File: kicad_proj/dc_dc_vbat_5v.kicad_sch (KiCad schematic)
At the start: 19 parts, among them Q1 DMG2305UX-7, U4 TPS563200, U7 DMMT5401-7-F

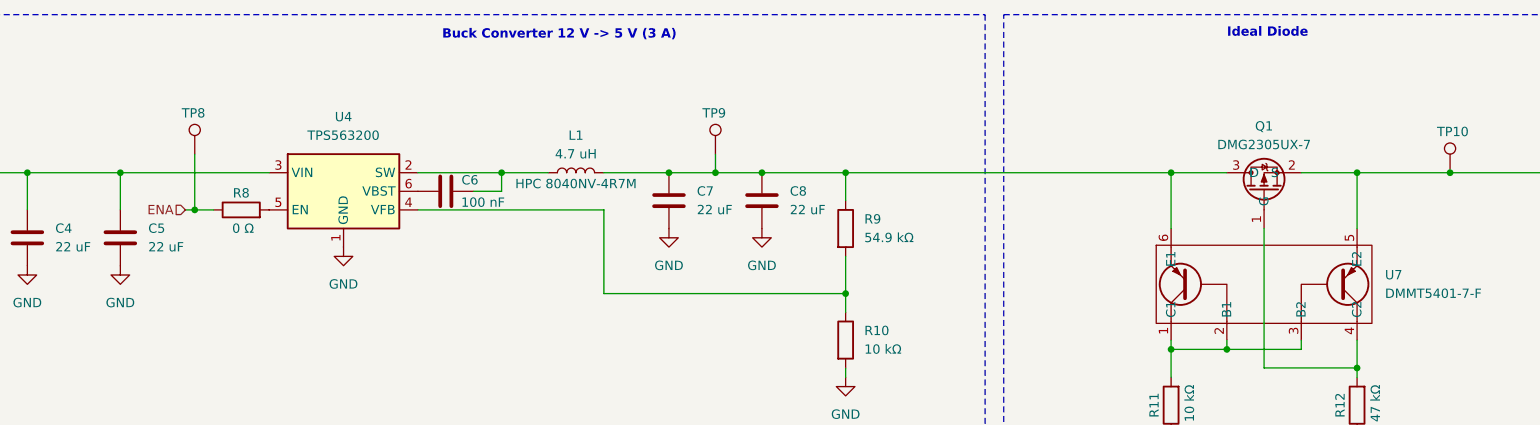
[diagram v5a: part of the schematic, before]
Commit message: progress a bit with the placement an replace 5 v buck converter L for a smaller one
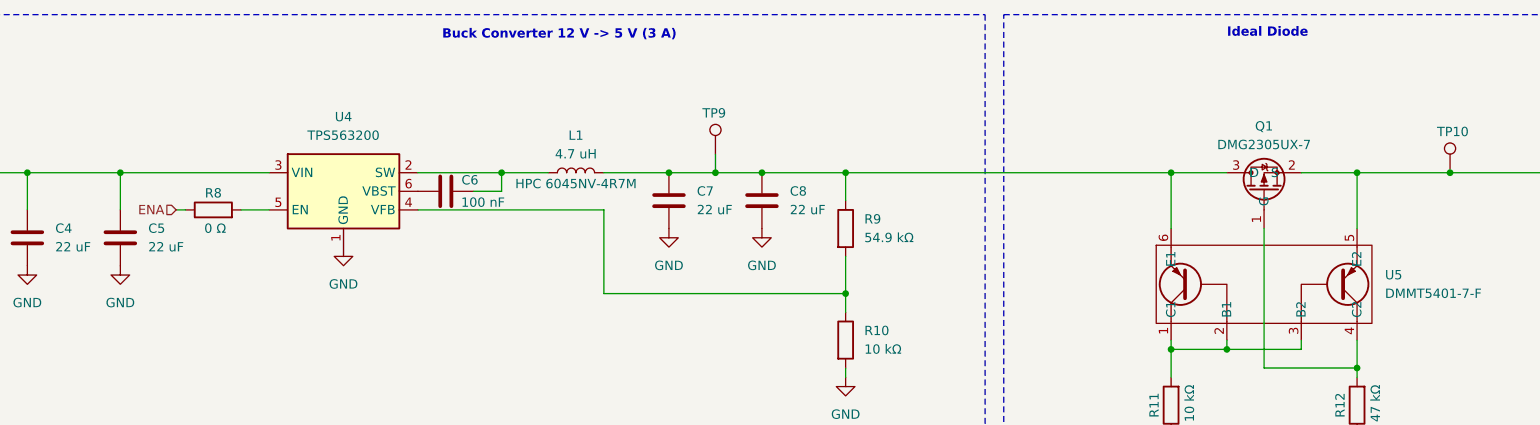
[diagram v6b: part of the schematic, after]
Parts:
- removed TP8: TestPoint, TestPoint:TestPoint_Pad_D2.5mm, symbol Connector:TestPoint
- L1: footprint rpi_power_warden_hat:L_8040_8x8x4mm -> rpi_power_warden_hat:L_6045_6x6x4mm; mpn HPC 8040NV-4R7M -> HPC 6045NV-4R7M
- renumbered U7 to U5
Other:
- moved on the sheet: R8
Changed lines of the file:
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@@
 	)
 	(junction
-		(at 69.85 90.17)
-		(diameter 0)
-		(color 0 0 0 0)
-	)
-	(junction
 		(at 228.6 111.76)
 		(diameter 0)
@@
 	(wire
 		(pts
-			(xy 68.58 90.17) (xy 69.85 90.17)
+			(xy 210.82 109.22) (xy 220.98 109.22)
 		)
 		(stroke
@@
 	(wire
 		(pts
-			(xy 210.82 109.22) (xy 220.98 109.22)
+			(xy 228.6 107.95) (xy 228.6 111.76)
 		)
 		(stroke
@@
 	(wire
 		(pts
-			(xy 228.6 107.95) (xy 228.6 111.76)
+			(xy 147.32 85.09) (xy 158.75 85.09)
 		)
 		(stroke
@@
 	(wire
 		(pts
-			(xy 147.32 85.09) (xy 158.75 85.09)
+			(xy 228.6 85.09) (xy 228.6 92.71)
 		)
 		(stroke
@@
 	(wire
 		(pts
-			(xy 228.6 85.09) (xy 228.6 92.71)
+			(xy 158.75 85.09) (xy 203.2 85.09)
 		)
 		(stroke
@@
 	(wire
 		(pts
-			(xy 158.75 85.09) (xy 203.2 85.09)
+			(xy 59.69 85.09) (xy 80.01 85.09)
 		)
 		(stroke
@@
 	(wire
 		(pts
-			(xy 59.69 85.09) (xy 80.01 85.09)
+			(xy 76.2 90.17) (xy 80.01 90.17)
 		)
 		(stroke
@@
 	(wire
 		(pts
+			(xy 67.31 90.17) (xy 68.58 90.17)
+		)
+		(stroke
+			(width 0)
+			(type default)
+		)
+	)
+	(wire
+		(pts
 			(xy 46.99 85.09) (xy 46.99 90.17)
 		)
@@
 	(wire
 		(pts
-			(xy 69.85 90.17) (xy 72.39 90.17)
-		)
-		(stroke
-			(width 0)
-			(type default)
-		)
-	)
-	(wire
-		(pts
 			(xy 228.6 85.09) (xy 241.3 85.09)
 		)
@@
 	(wire
 		(pts
-			(xy 69.85 82.55) (xy 69.85 90.17)
-		)
-		(stroke
-			(width 0)
-			(type default)
-		)
-	)
-	(wire
-		(pts
 			(xy 158.75 96.52) (xy 158.75 101.6)
 		)
@@
 	(hierarchical_label "ENA"
 		(shape input)
-		(at 68.58 90.17 180)
+		(at 67.31 90.17 180)
 		(effects
 			(font
@@
 		(dnp no)
 		(fields_autoplaced yes)
-		(property "Reference" "U7"
+		(property "Reference" "U5"
 			(at 232.41 99.0599 0)
 			(effects
@@
 	)
 	(symbol
-		(lib_id "Connector:TestPoint")
-		(at 69.85 82.55 0)
-		(unit 1)
-		(exclude_from_sim no)
-		(in_bom no)
-		(on_board yes)
-		(dnp no)
-		(property "Reference" "TP8"
-			(at 68.072 76.962 0)
-			(effects
-				(font
-					(size 1.27 1.27)
-				)
-				(justify left)
-			)
-		)
-		(property "Value" "TestPoint"
-			(at 72.39 80.5179 0)
-			(effects
-				(font
-					(size 1.27 1.27)
-				)
-				(justify left)
-				(hide yes)
-			)
-		)
-		(property "Footprint" "TestPoint:TestPoint_Pad_D2.5mm"
-			(at 74.93 82.55 0)
-			(effects
-				(font
-					(size 1.27 1.27)
-				)
-				(hide yes)
-			)
-		)
-		(property "Datasheet" "~"
-			(at 74.93 82.55 0)
-			(effects
-				(font
-					(size 1.27 1.27)
-				)
-				(hide yes)
-			)
-		)
-		(property "Description" "test point"
-			(at 69.85 82.55 0)
-			(effects
-				(font
-					(size 1.27 1.27)
-				)
-				(hide yes)
-			)
-		)
-		(pin "1"
-		)
-		(instances
-			(project "rpi_power_warden_hat"
-				(path "/8692c5de-a943-41e8-8e29-f6c5e99cda34/5bbc6f2d-46db-4213-8835-1ada71ba8330"
-					(reference "TP8")
-					(unit 1)
-				)
-				(path "/8692c5de-a943-41e8-8e29-f6c5e99cda34/cc58a92a-1392-4aa4-91cc-7a70ded8904f"
-					(reference "TP11")
-					(unit 1)
-				)
-			)
-		)
-	)
-	(symbol
 		(lib_id "power:GND")
 		(at 46.99 97.79 0)
@@
 	(symbol
 		(lib_id "Device:R")
-		(at 76.2 90.17 90)
+		(at 72.39 90.17 90)
 		(unit 1)
 		(exclude_from_sim no)
@@
 		(dnp no)
 		(property "Reference" "R8"
-			(at 76.2 87.884 90)
+			(at 72.39 87.884 90)
 			(effects
 				(font
@@
 		)
 		(property "Value" "0 Ω"
-			(at 76.454 92.71 90)
+			(at 72.644 92.71 90)
 			(effects
 				(font
@@
 		)
 		(property "Footprint" "Resistor_SMD:R_0603_1608Metric_Pad0.98x0.95mm_HandSolder"
-			(at 76.2 91.948 90)
+			(at 72.39 91.948 90)
 			(effects
 				(font
@@
 		)
 		(property "Datasheet" "~"
-			(at 76.2 90.17 0)
+			(at 72.39 90.17 0)
 			(effects
 				(font
@@
 		)
 		(property "Description" "RES SMD 0 OHM JUMPER 1/10W 0603"
-			(at 76.2 90.17 0)
+			(at 72.39 90.17 0)
 			(effects
 				(font
@@
 		)
 		(property "mpn" "ERJ-3GEY0R00V"
-			(at 76.2 90.17 0)
+			(at 72.39 90.17 0)
 			(effects
 				(font
@@
 		)
 		(property "manufacturer" "Panasonic Electronic Components"
-			(at 76.2 90.17 0)
+			(at 72.39 90.17 0)
 			(effects
 				(font
@@
 			)
 		)
-		(property "Footprint" "rpi_power_warden_hat:L_8040_8x8x4mm"
+		(property "Footprint" "rpi_power_warden_hat:L_6045_6x6x4mm"
 			(at 121.92 85.09 0)
 			(effects
@@
 			)
 		)
-		(property "Description" "HPC 8040NV-4R7M"
+		(property "Description" "FIXED IND 4.7UH 4A 0.026OHM SMD"
 			(at 121.92 85.09 0)
 			(effects
@@
 			)
 		)
-		(property "mpn" "HPC 8040NV-4R7M"
+		(property "mpn" "HPC 6045NV-4R7M"
 			(at 121.92 86.614 90)
 			(effects

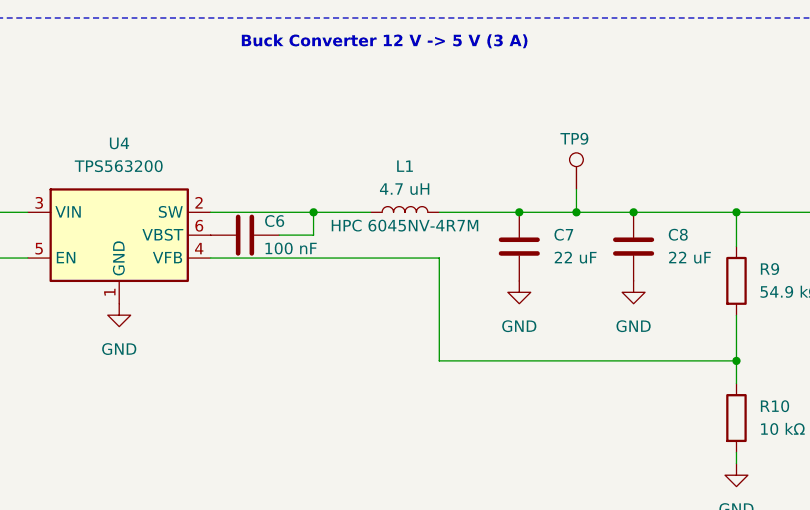
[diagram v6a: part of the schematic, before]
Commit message: fix: replace some components out of stock in lcsc
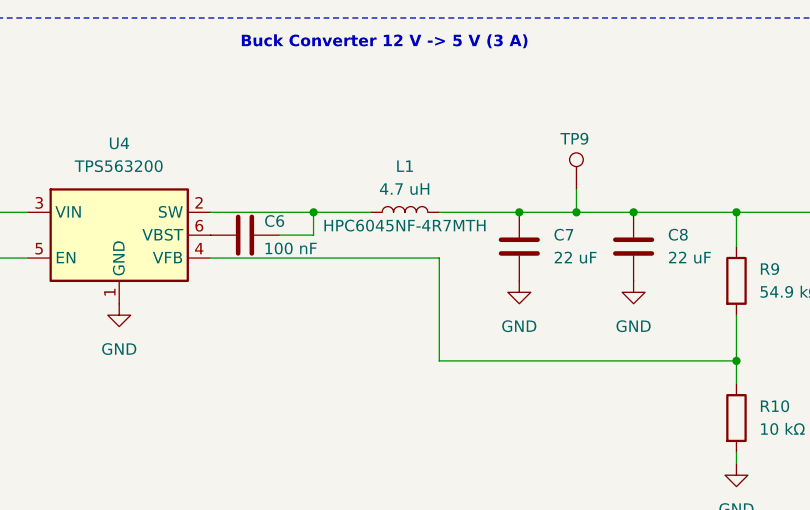
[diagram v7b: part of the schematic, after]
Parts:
- L1: manufacturer_2 (none) -> TAI-TECH Advanced Electronics Co., Ltd.; mpn HPC 6045NV-4R7M -> HPC6045NF-4R7MTH; mpn_2 (none) -> HPC 6045NV-4R7M
- R9: manufacturer Panasonic Electronic Components -> UNI-ROYAL(Uniroyal Elec); manufacturer_2 (none) -> Panasonic Electronic Components; mpn ERJ-3EKF5492V -> 0603WAF5492T5E; mpn_2 (none) -> ERJ-3EKF5492V
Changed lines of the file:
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@@
 			)
 		)
-		(property "mpn" "ERJ-3EKF5492V"
+		(property "mpn_2" "ERJ-3EKF5492V"
 			(at 158.75 92.71 0)
 			(effects
@@
 			)
 		)
-		(property "manufacturer" "Panasonic Electronic Components"
+		(property "manufacturer_2" "Panasonic Electronic Components"
+			(at 158.75 92.71 0)
+			(effects
+				(font
+					(size 1.27 1.27)
+				)
+				(hide yes)
+			)
+		)
+		(property "mpn" "0603WAF5492T5E"
+			(at 158.75 92.71 0)
+			(effects
+				(font
+					(size 1.27 1.27)
+				)
+				(hide yes)
+			)
+		)
+		(property "manufacturer" "UNI-ROYAL(Uniroyal Elec)"
 			(at 158.75 92.71 0)
 			(effects
@@
 			)
 		)
-		(property "Description" "FIXED IND 4.7UH 4A 0.026OHM SMD"
+		(property "Description" "4A 4.7uH ±20% SMD Power Inductors ROHS"
 			(at 121.92 85.09 0)
 			(effects
@@
 				)
 				(hide yes)
+			)
+		)
+		(property "manufacturer_2" "TAI-TECH Advanced Electronics Co., Ltd."
+			(at 121.92 85.09 90)
+			(effects
+				(font
+					(size 1.27 1.27)
+				)
+				(hide yes)
+			)
+		)
+		(property "mpn_2" "HPC 6045NV-4R7M"
+			(at 121.92 86.614 90)
+			(effects
+				(font
+					(size 1.27 1.27)
+				)
+				(hide yes)
+			)
+		)
+		(property "mpn" "HPC6045NF-4R7MTH"
+			(at 121.92 86.614 90)
+			(effects
+				(font
+					(size 1.27 1.27)
+				)
 			)
 		)
@@
 			)
 		)
-		(property "mpn" "HPC 6045NV-4R7M"
-			(at 121.92 86.614 90)
-			(effects
-				(font
-					(size 1.27 1.27)
-				)
-			)
-		)
